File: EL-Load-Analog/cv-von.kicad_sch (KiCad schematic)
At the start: 50 parts, among them Q3 MMBT5551, Q5 MMBT5401, Q6 MMBT5551, Q8 MMBT5401, U2 LM393, U401 AD8038, U402 LM393, U403 74HCT02

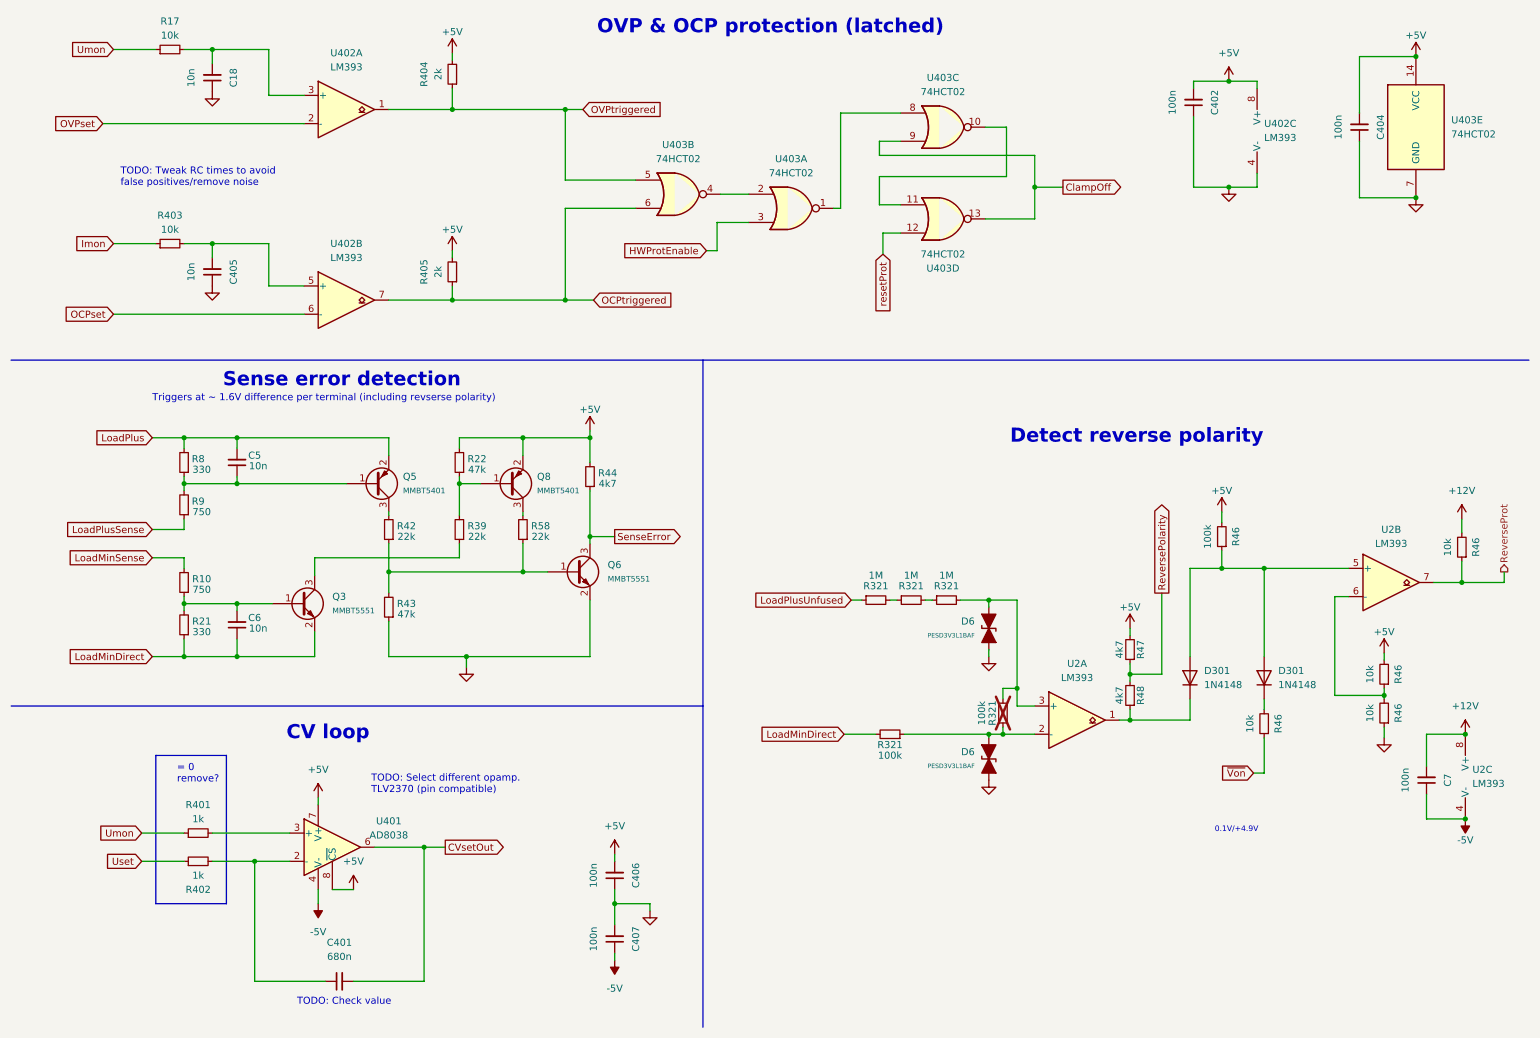
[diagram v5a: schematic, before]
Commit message: Changed comparator to LM393A.
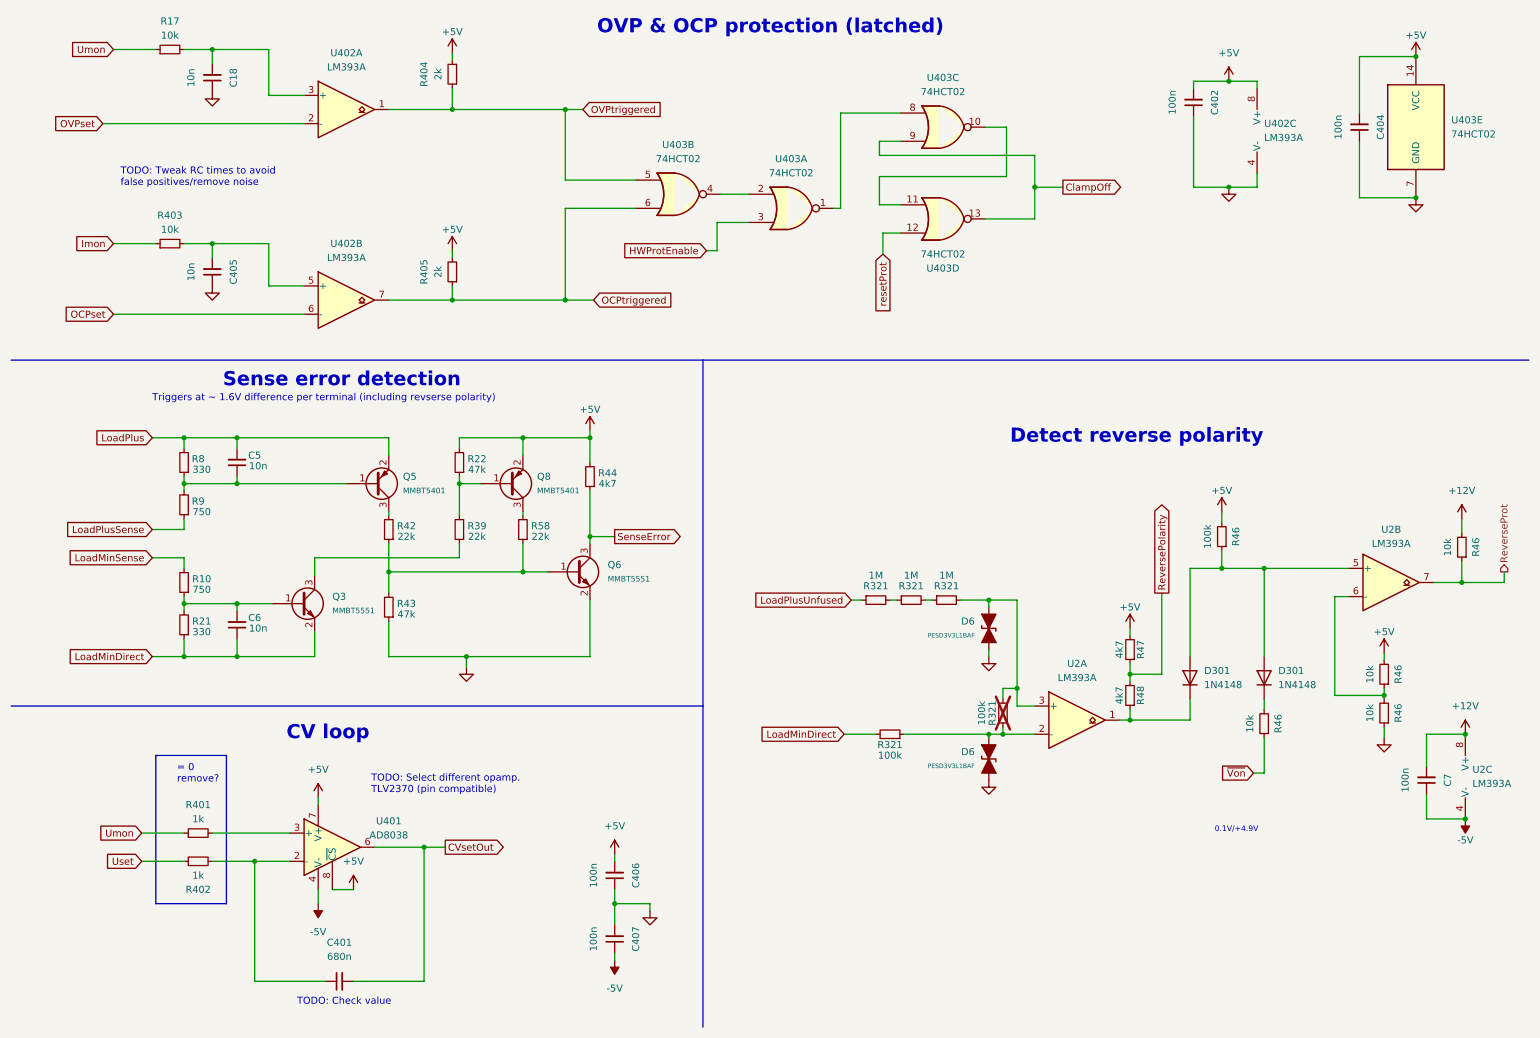
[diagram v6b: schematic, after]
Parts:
- U2, U402: value LM393 -> LM393A; Part Name U_LM393 -> U_LM393A
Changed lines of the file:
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@@
       (effects (font (size 1.27 1.27)))
     )
-    (property "Value" "LM393" (at 72.39 25.4 0)
+    (property "Value" "LM393A" (at 72.39 25.4 0)
       (effects (font (size 1.27 1.27)))
     )
@@
       (effects (font (size 1.27 1.27)) hide)
     )
-    (property "Part Name" "U_LM393 " (at 72.39 33.02 0)
+    (property "Part Name" "U_LM393A" (at 72.39 33.02 0)
       (effects (font (size 1.27 1.27)) hide)
     )
@@
       (effects (font (size 1.27 1.27)))
     )
-    (property "Value" "LM393" (at 72.39 59.69 0)
+    (property "Value" "LM393A" (at 72.39 59.69 0)
       (effects (font (size 1.27 1.27)))
     )
@@
       (effects (font (size 1.27 1.27)) hide)
     )
-    (property "Part Name" "U_LM393 " (at 72.39 67.31 0)
+    (property "Part Name" "U_LM393A" (at 72.39 67.31 0)
       (effects (font (size 1.27 1.27)) hide)
     )
@@
       (effects (font (size 1.27 1.27)))
     )
-    (property "Value" "LM393" (at 203.835 135.255 0)
+    (property "Value" "LM393A" (at 203.835 135.255 0)
       (effects (font (size 1.27 1.27)))
     )
@@
       (effects (font (size 1.27 1.27)) hide)
     )
-    (property "Part Name" "U_LM393 " (at 203.835 142.875 0)
+    (property "Part Name" "U_LM393A" (at 203.835 142.875 0)
       (effects (font (size 1.27 1.27)) hide)
     )
@@
       (effects (font (size 1.27 1.27)))
     )
-    (property "Value" "LM393" (at 260.35 111.125 0)
+    (property "Value" "LM393A" (at 260.35 111.125 0)
       (effects (font (size 1.27 1.27)))
     )
@@
       (effects (font (size 1.27 1.27)) hide)
     )
-    (property "Part Name" "U_LM393 " (at 260.35 118.11 0)
+    (property "Part Name" "U_LM393A" (at 260.35 118.11 0)
       (effects (font (size 1.27 1.27)) hide)
     )
@@
       (effects (font (size 1.27 1.27)) (justify left))
     )
-    (property "Value" "LM393" (at 237.49 38.0999 0)
+    (property "Value" "LM393A" (at 237.49 38.0999 0)
       (effects (font (size 1.27 1.27)) (justify left))
     )
@@
       (effects (font (size 1.27 1.27)) hide)
     )
-    (property "Part Name" "U_LM393 " (at 238.76 36.83 0)
+    (property "Part Name" "U_LM393A" (at 238.76 36.83 0)
       (effects (font (size 1.27 1.27)) hide)
     )
@@
       (effects (font (size 1.27 1.27)) (justify left))
     )
-    (property "Value" "LM393" (at 274.955 154.305 0)
+    (property "Value" "LM393A" (at 274.955 154.305 0)
       (effects (font (size 1.27 1.27)) (justify left))
     )
@@
       (effects (font (size 1.27 1.27)) hide)
     )
-    (property "Part Name" "U_LM393 " (at 276.225 153.035 0)
-      (effects (font (size 1.27 1.27)) hide)
-    )
+    (property "Part Name" "U_LM393A" (at 276.225 153.035 0)
+      (effects (font (size 1.27 1.27)) hide)
+    )
